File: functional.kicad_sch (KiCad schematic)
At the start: 20 parts, among them J1 PPTC061LFBN-RC, J5 TSW-102-23-T-S, SW1 SW_Push, U5 W25Q128JVSIQ, U6 USB3343-CP-TR

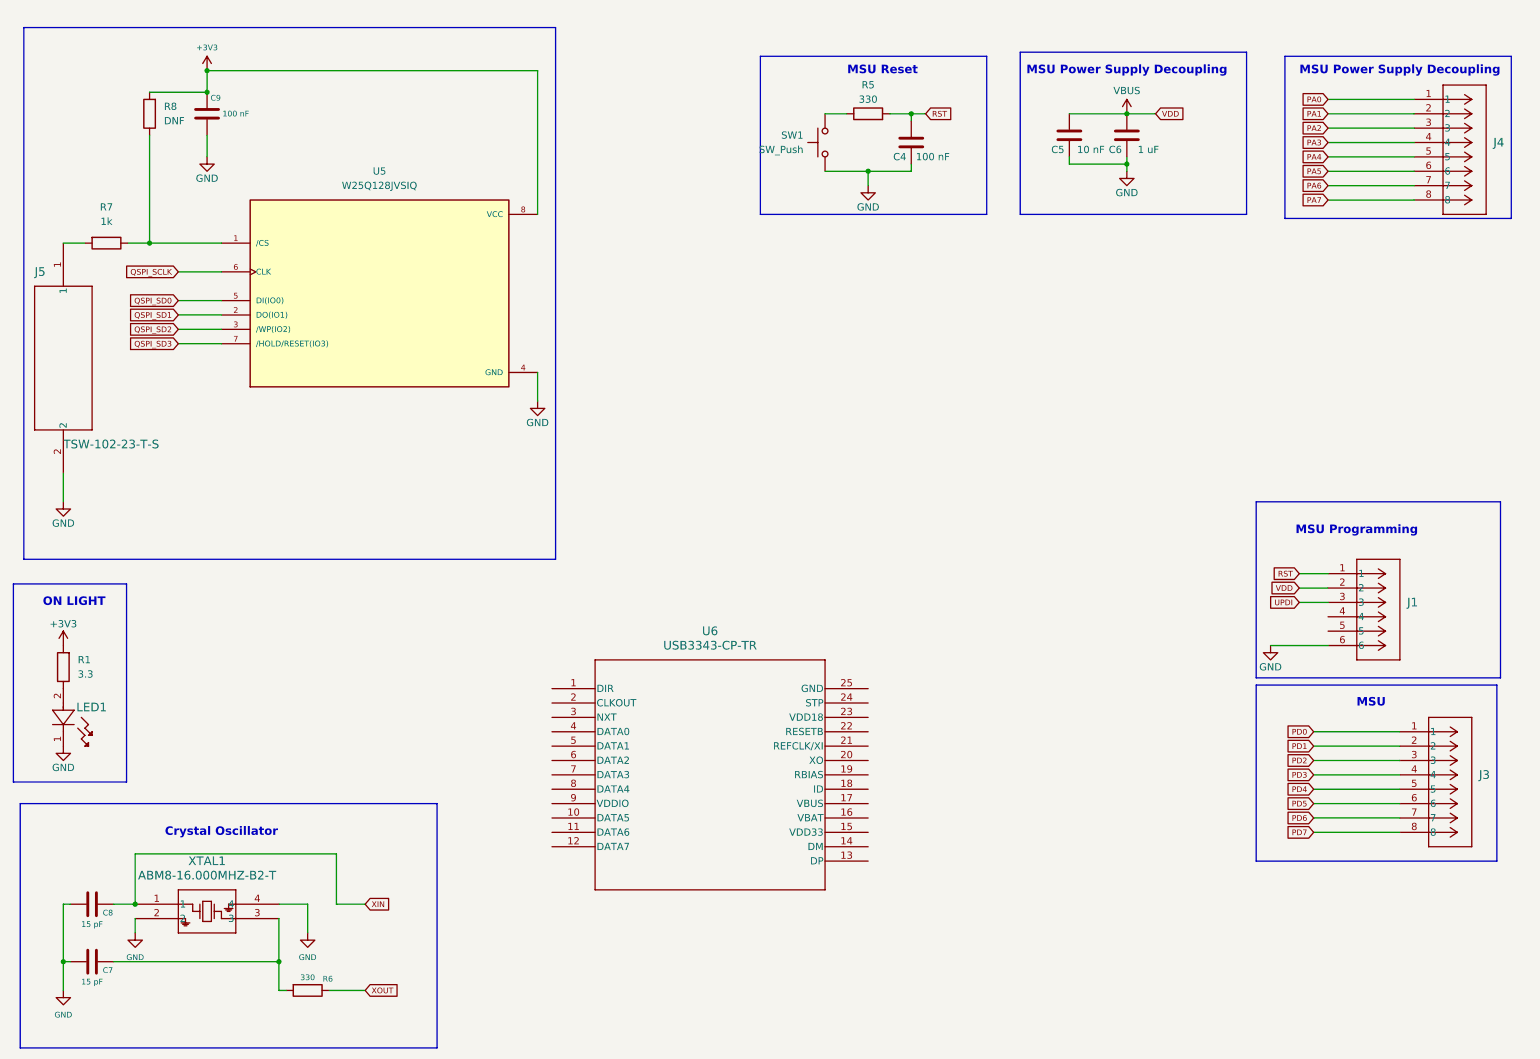
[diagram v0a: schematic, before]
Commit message: finished ERC, matched footprints, populated 3D models
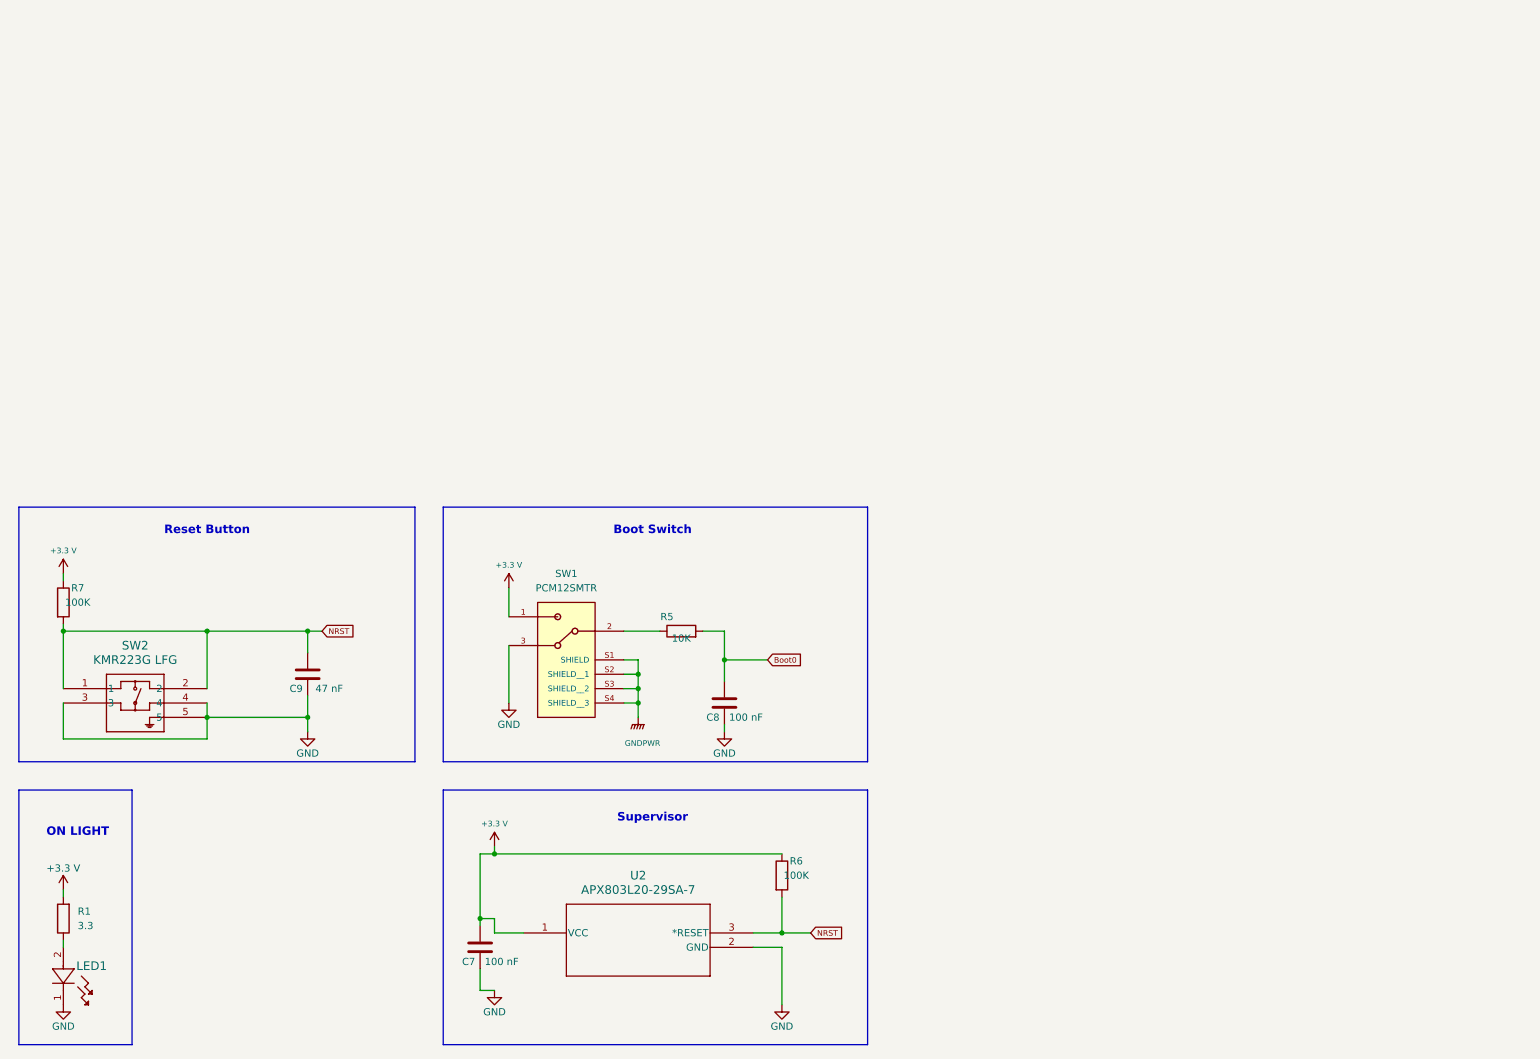
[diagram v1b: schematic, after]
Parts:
- removed C4: 100 nF, Capacitor_SMD:C_0805_2012Metric, symbol Device:C
- removed C5: 10 nF, Capacitor_SMD:C_0805_2012Metric, symbol Device:C
- removed C6: 1 uF, Capacitor_SMD:C_0805_2012Metric, symbol Device:C
- removed J1: PPTC061LFBN-RC, CONN6_061LFBN-RC_SUL, symbol PPTC061LFBN_RC:PPTC061LFBN-RC
- removed J3, J4: ~, CONN_PPTC081LFBN-RC_SUL, symbol PPTC081LFBN_RC:PPTC081LFBN-RC
- removed J5: TSW-102-23-T-S, TSW-102-23-G-S_SAI, symbol TSW_102_23_T_S:TSW-102-23-T-S
- removed R8: DNF, Resistor_SMD:R_0805_2012Metric, symbol Device:R
- removed SW1: SW_Push, symbol Switch:SW_Push
- removed U5: W25Q128JVSIQ, W25Q128JVSIQ:SOIC127P790X216-8N, symbol W25Q128JVSIQ:W25Q128JVSIQ
- removed U6: USB3343-CP-TR, QFN24_4X4MC_MCH, symbol USB3343_CP_TR:USB3343-CP-TR
- removed XTAL1: ABM8-16.000MHZ-B2-T, ABM8_ABR, symbol ABM8:ABM8-16.000MHZ-B2-T
- added SW1: PCM12SMTR, PCM12SMTR:PCM12SMTR_CNK, symbol PCM12SMTR:PCM12SMTR
- added SW2: KMR223G LFG, KMR223_LFG:KMR2_G_CNK, symbol KMR223G:KMR223G_LFG
- added U2: APX803L20-29SA-7, APX803L20-29-SA-7:SOT23_SA_DIO, symbol APX803L20_29SA_7:APX803L20-29SA-7
- C7, C8: value 15 pF -> 100 nF
- C9: value 100 nF -> 47 nF
- LED1: footprint LEDBS75000_WRE:LED_BS75000_WRE -> 150080BS75000:LED_BS75000_WRE
- R5: value 330 -> 10K
- R6: value 330 -> 100K
- R7: value 1k -> 100K
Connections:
- net XIN is gone; now on net GND: C8.1
- net XOUT is gone; now on net +3.3 V: R6.1
- net GND: now also C7.1, C9.1, SW1.3, SW2.3, SW2.4, SW2.5, U2.2 (GND); no longer C7.2, C8.2, C9.2
- net NRST: now reaches R7.2
- net NRST: now also C9.2, R6.2, SW2.1, SW2.2, U2.3 (*RESET)
- net at R5.1: now also SW1.2
- net +3.3 V: now reaches R7.1
- net +3.3 V: now also C7.2, R1.2, SW1.1, U2.1 (VCC)
- removed net +3V3: C9.1, R1.2
- net RST renamed Boot0
- net Boot0: now also C8.2
- new net GNDPWR: SW1.S1 (SHIELD), SW1.S2 (SHIELD__1), SW1.S3 (SHIELD__2), SW1.S4 (SHIELD__3)
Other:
- note added: "Boot Switch"
- note added: "Reset Button"
- note added: "Supervisor"
- note removed: "Crystal Oscillator"
- note removed: "MSU"
- note removed: "MSU Power Supply Decoupling"
- note removed: "MSU Programming"
- note removed: "MSU Reset"
- moved on the sheet: LED1, R1

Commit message: matched footprint name to name of component
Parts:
- LED1: footprint 150080BS75000:LED_BS75000_WRE -> 150080BS75000:150080BS75000
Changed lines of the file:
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@@
 			)
 		)
-		(property "Footprint" "150080BS75000:LED_BS75000_WRE"
+		(property "Footprint" "150080BS75000:150080BS75000"
 			(at 19.05 177.8 0)
 			(effects

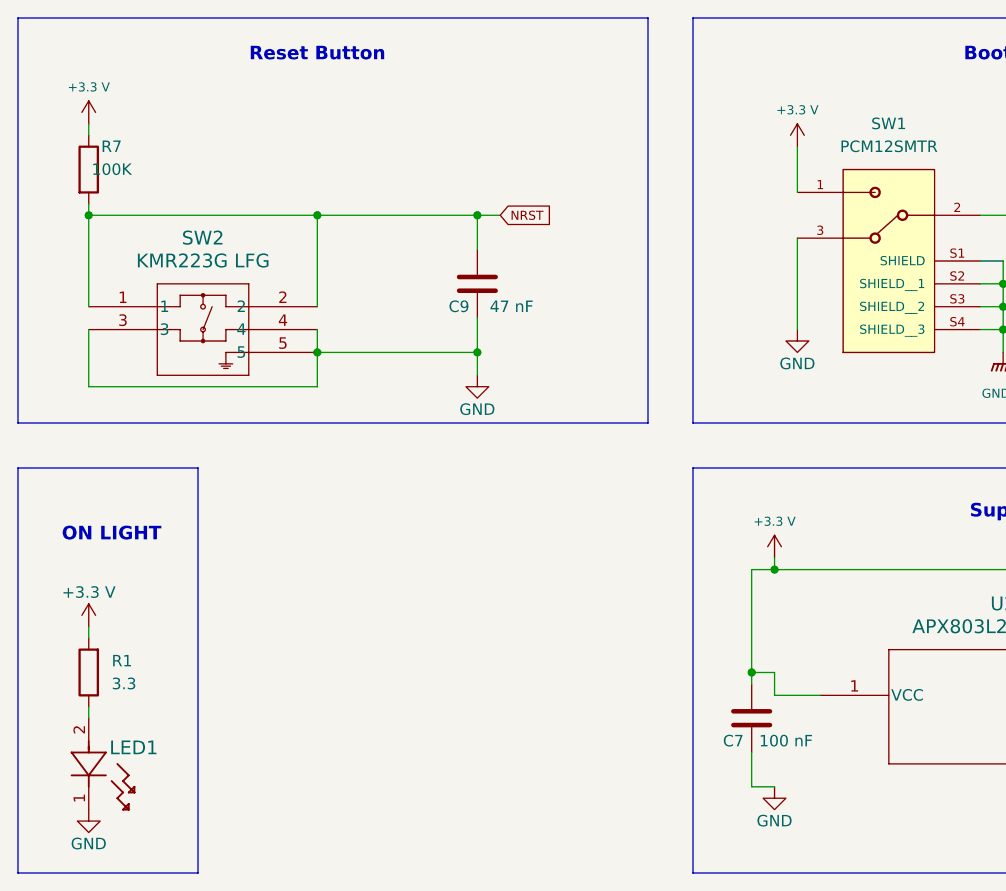
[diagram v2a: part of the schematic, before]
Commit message: removed manual switch
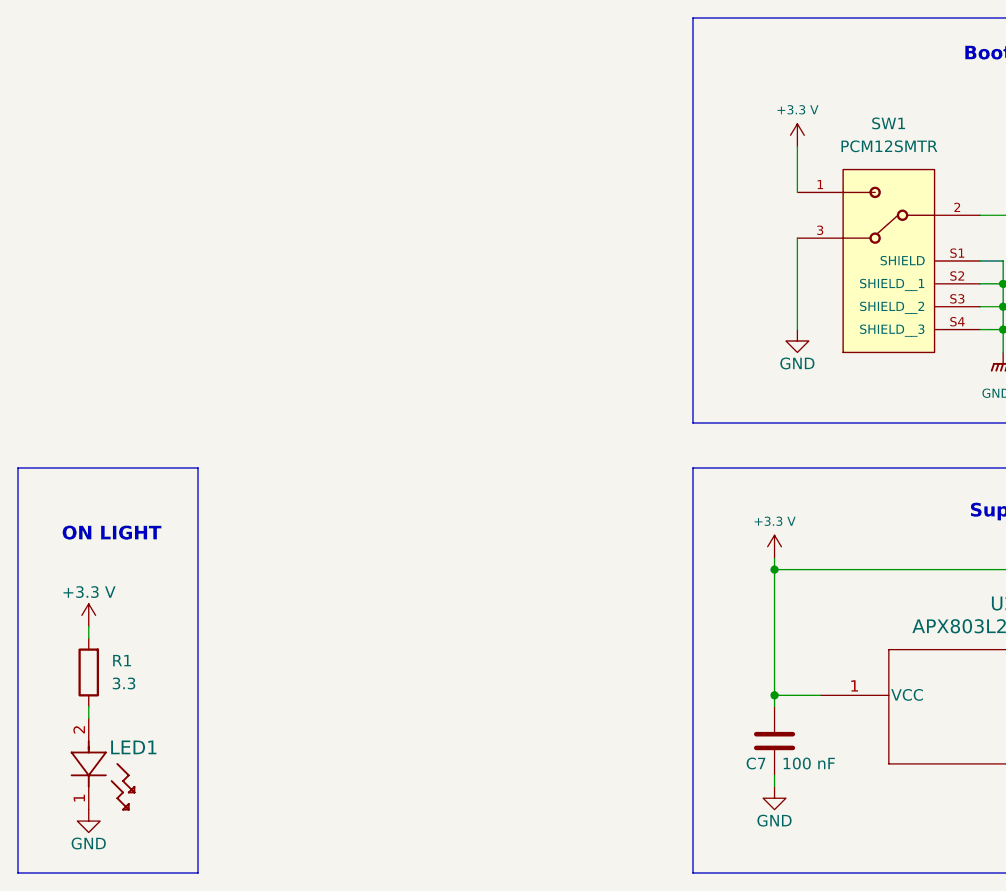
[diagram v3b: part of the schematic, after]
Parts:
- removed C9: 47 nF, Capacitor_SMD:C_0805_2012Metric, symbol Device:C
- removed R7: 100K, Resistor_SMD:R_0805_2012Metric, symbol Device:R
- removed SW2: KMR223G LFG, KMR223_LFG:KMR2_G_CNK, symbol KMR223G:KMR223G_LFG
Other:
- note removed: "Reset Button"
- moved on the sheet: C7

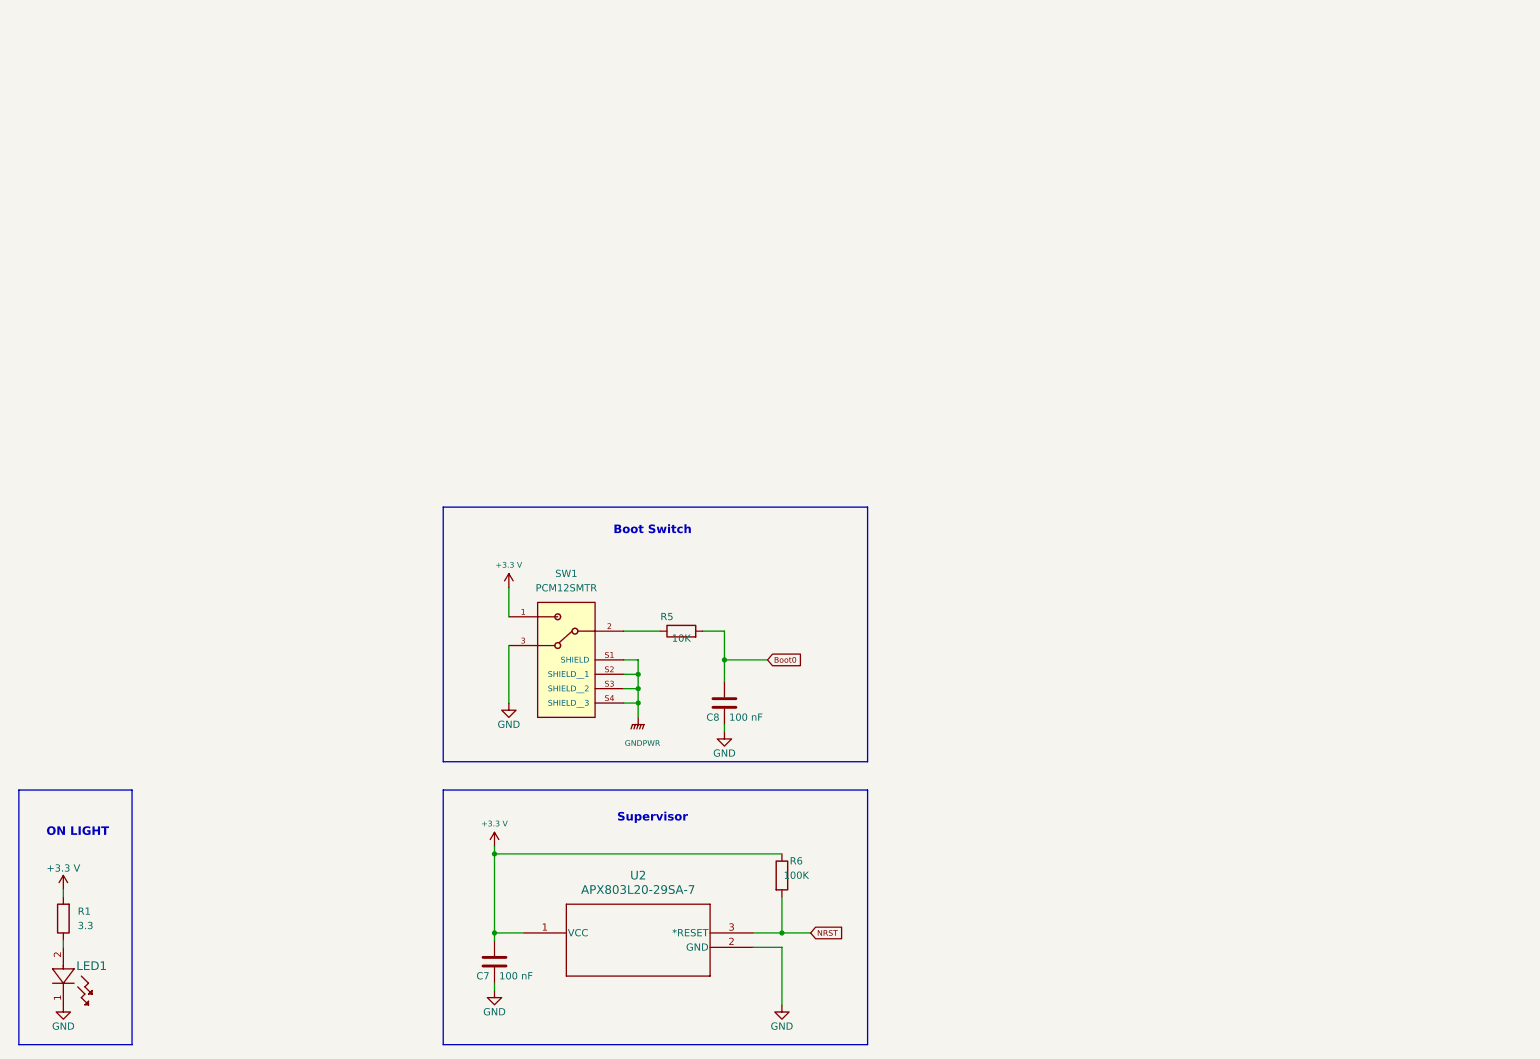
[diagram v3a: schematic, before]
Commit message: removed AVR mcu
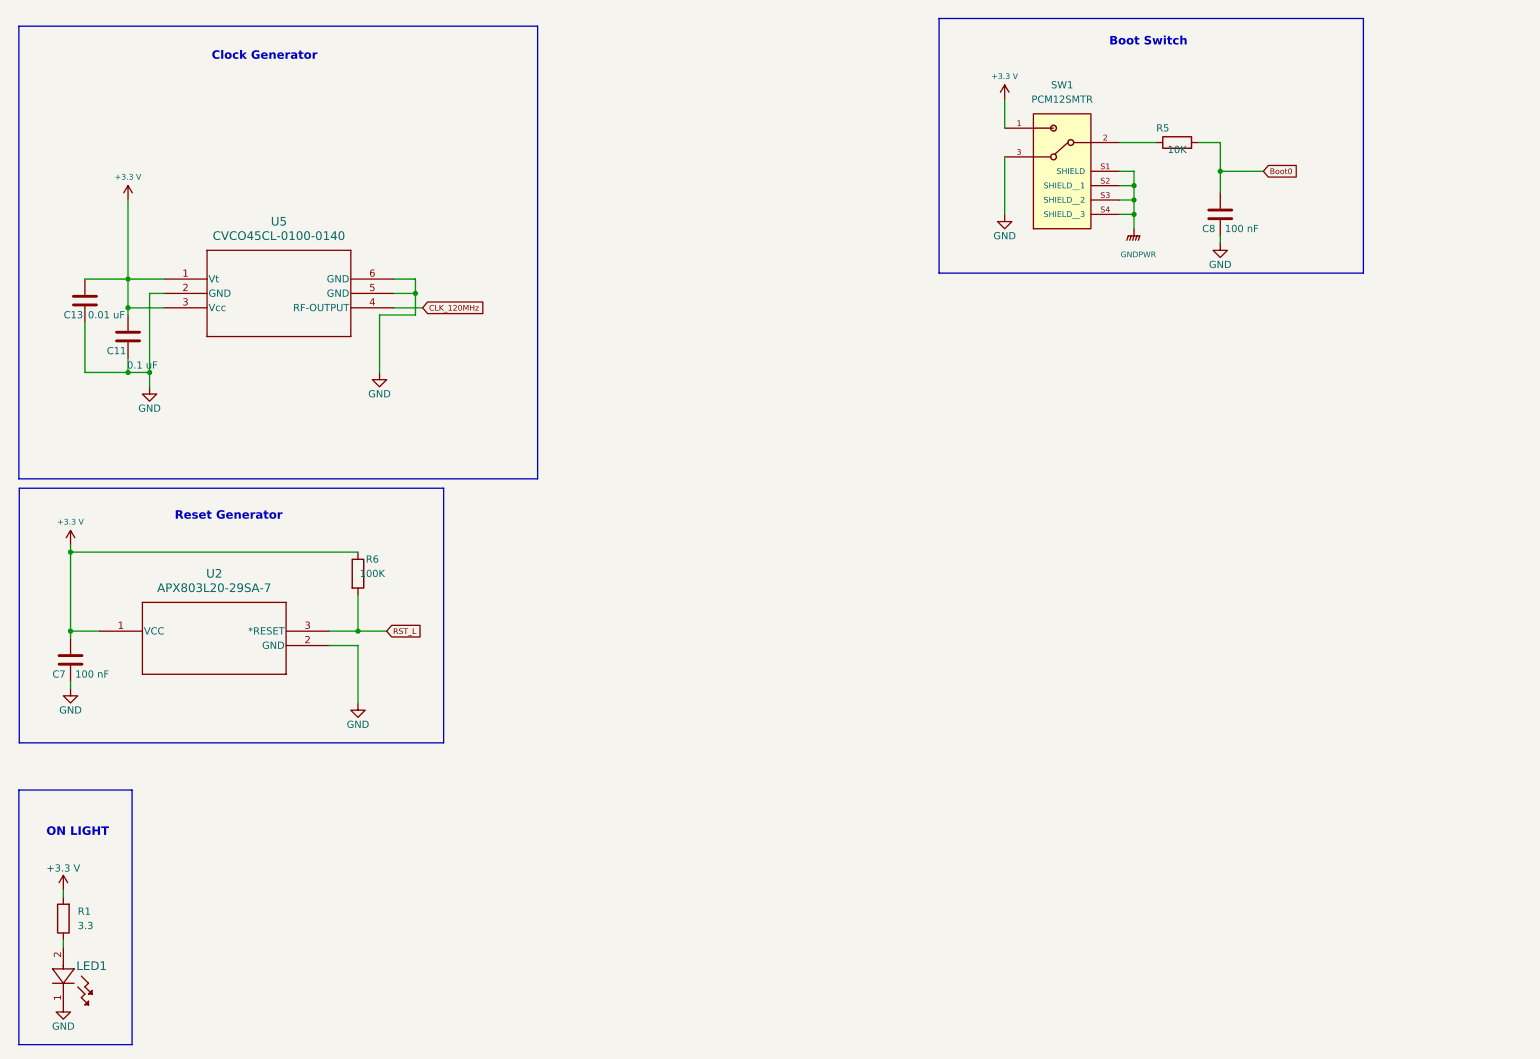
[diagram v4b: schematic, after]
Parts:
- added C11: 0.1 uF, Capacitor_SMD:C_0805_2012Metric, symbol Device:C
- added C13: 0.01 uF, Capacitor_SMD:C_0805_2012Metric, symbol Device:C
- added U5: CVCO45CL-0100-0140, _CVCO45CL-0100-0140_CRX, symbol VCO_120MHZ:CVCO45CL-0100-0140
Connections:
- net +3.3 V: now also C11.2, C13.2, U5.1 (Vt), U5.3 (Vcc)
- net GND: now also C11.1, C13.1, U5.2 (GND), U5.5 (GND), U5.6 (GND)
- net NRST renamed RST_L
- new net CLK_120MHz: U5.4 (RF-OUTPUT)
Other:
- note added: "Clock Generator"
- note added: "Reset Generator"
- note removed: "Supervisor"
- moved on the sheet: C7, C8, R5, R6, SW1, U2

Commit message: added diode
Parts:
- removed C11: 0.1 uF, Capacitor_SMD:C_0805_2012Metric, symbol Device:C
- removed C13: 0.01 uF, Capacitor_SMD:C_0805_2012Metric, symbol Device:C
- removed U5: CVCO45CL-0100-0140, _CVCO45CL-0100-0140_CRX, symbol VCO_120MHZ:CVCO45CL-0100-0140
- added C12, C9: 8 pF, Capacitor_SMD:C_0805_2012Metric, symbol Device:C
- added U3: PL500-37TC, SOP-8_MCH, symbol VCO_36MHZ:PL500-37TC
- added Y1: XRCGB32M000F2P01R0, XRCGB32M000F2P01R0:OSC_XRCGB32M000F2P01R0, symbol XRCGB32M000F2P01R0:XRCGB32M000F2P01R0
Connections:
- net GND: now also C12.1, C9.1, U3.4 (GND)
- net +3.3 V renamed VBOARD
- net VBOARD: now also U3.2 (*OE), U3.3 (VCON), U3.6 (VDD)
- new net CLK_32MHZ: U3.5 (CLK)
- new net XIN: C9.2, U3.1 (XIN), Y1.1
- new net XOUT: C12.2, U3.8 (XOUT), Y1.3
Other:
- note added: "High-Speed Crystal"
- note added: "Voltage-Controlled Oscillator"
- note removed: "Clock Generator"
- moved on the sheet: C8, R5, SW1
